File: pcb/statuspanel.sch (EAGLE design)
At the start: 3 parts

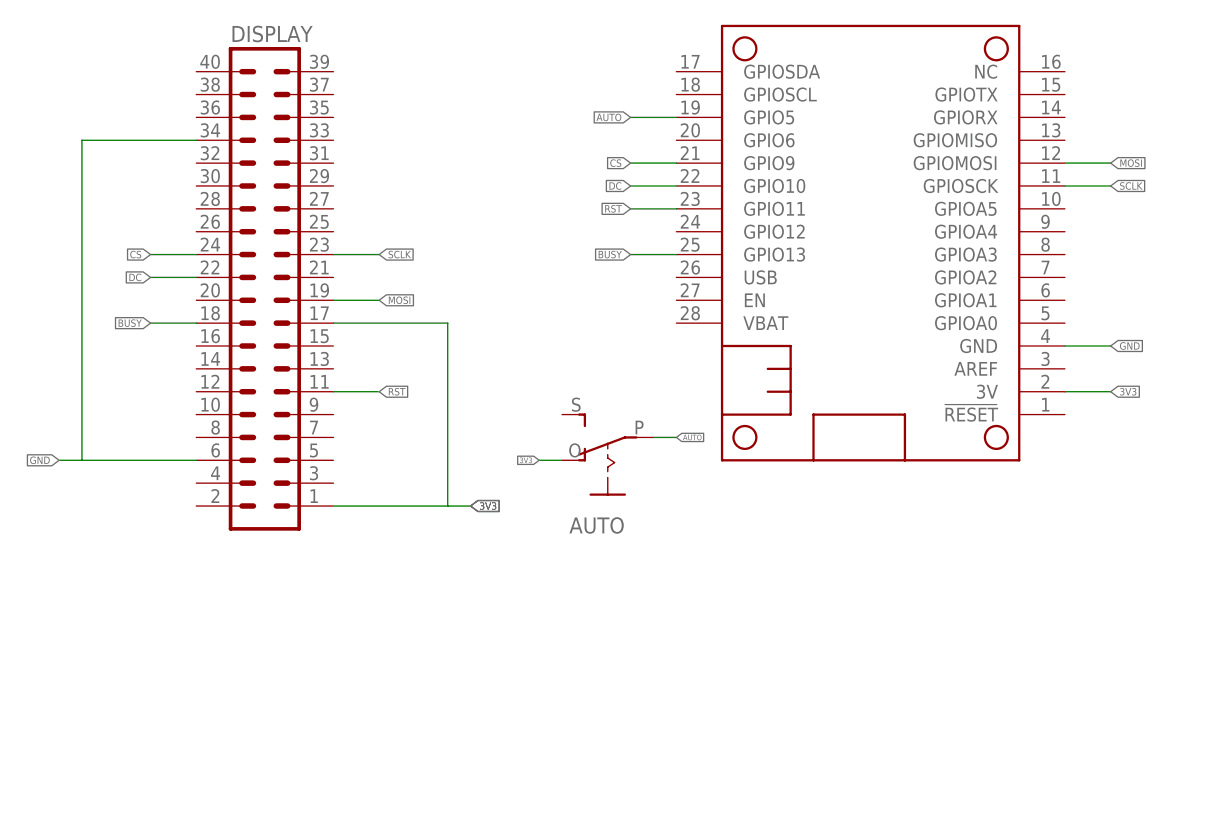
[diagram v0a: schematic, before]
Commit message: Update the PCB to add an unpair button
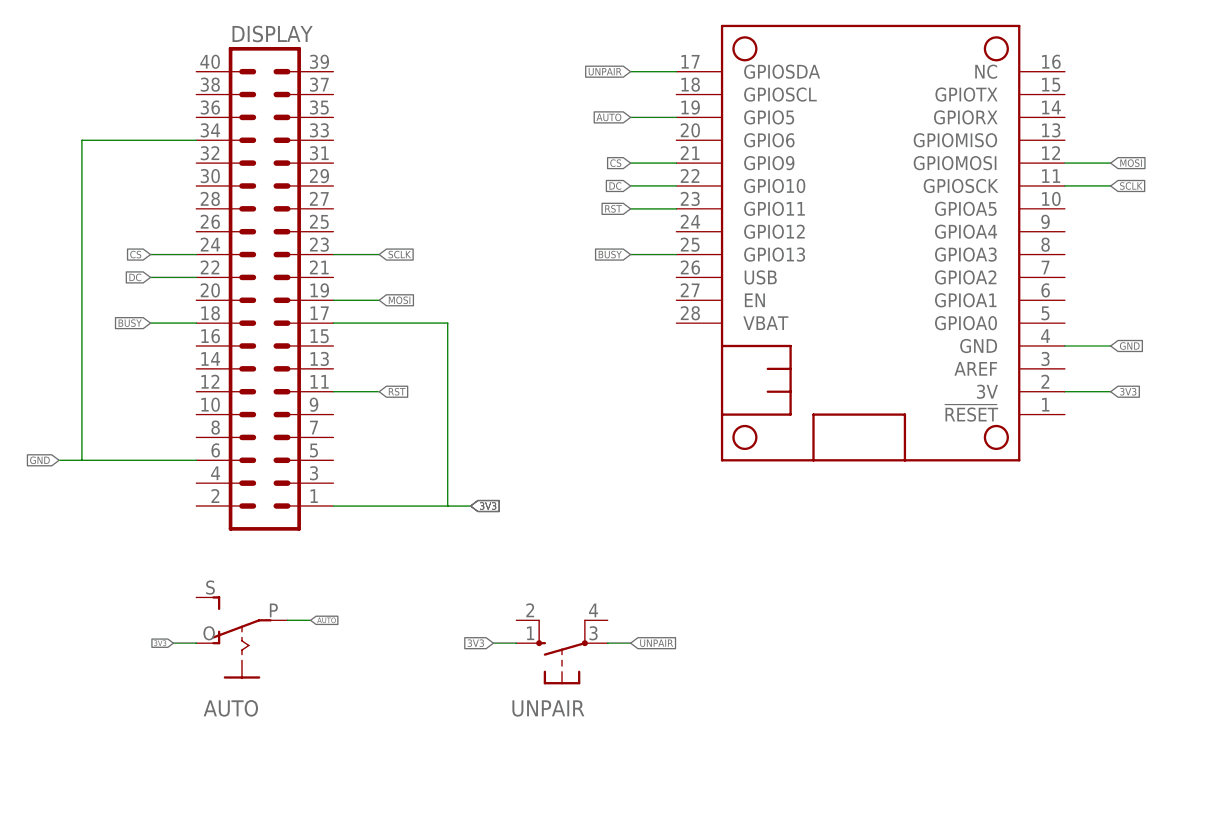
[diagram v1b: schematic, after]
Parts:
- added UNPAIR: (no value), switch-omron:10-XX
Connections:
- new net UNPAIR: HUZZAH32.GPIOSDA, UNPAIR.P
- net 3V3: now also UNPAIR.S
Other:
- moved on the sheet: AUTO
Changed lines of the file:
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@@
 <?xml version="1.0" encoding="utf-8"?>
 <!DOCTYPE eagle SYSTEM "eagle.dtd">
-<eagle version="9.2.2">
+<eagle version="9.5.2">
 <drawing>
 <settings>
@@
 <part name="DISPLAY" library="con-lstb" library_urn="urn:adsk.eagle:library:162" deviceset="MA20-2" device="" package3d_urn="urn:adsk.eagle:package:8338/1"/>
 <part name="AUTO" library="adafruit" library_urn="urn:adsk.eagle:library:420" deviceset="EG1218" device="S" package3d_urn="urn:adsk.eagle:package:6240649/1"/>
+<part name="UNPAIR" library="switch-omron" library_urn="urn:adsk.eagle:library:377" deviceset="10-XX" device="" package3d_urn="urn:adsk.eagle:package:27496/1"/>
 </parts>
 <sheets>
@@
 <attribute name="NAME" x="41.91" y="89.662" size="1.778" layer="95"/>
 </instance>
-<instance part="AUTO" gate="1" x="83.82" y="43.18" smashed="yes" rot="R90">
-<attribute name="NAME" x="85.725" y="36.83" size="1.778" layer="95" rot="R180"/>
-<attribute name="VALUE" x="80.645" y="39.37" size="1.778" layer="96" rot="R180"/>
+<instance part="AUTO" gate="1" x="43.18" y="22.86" smashed="yes" rot="R90">
+<attribute name="NAME" x="45.085" y="16.51" size="1.778" layer="95" rot="R180"/>
+<attribute name="VALUE" x="40.005" y="19.05" size="1.778" layer="96" rot="R180"/>
+</instance>
+<instance part="UNPAIR" gate="1" x="78.74" y="22.86" smashed="yes" rot="R90">
+<attribute name="NAME" x="81.28" y="16.51" size="1.778" layer="95" rot="R180"/>
+<attribute name="VALUE" x="75.565" y="19.05" size="1.778" layer="96" rot="R180"/>
 </instance>
 </instances>
@@
 <segment>
 <pinref part="AUTO" gate="1" pin="O"/>
-<wire x1="78.74" y1="43.18" x2="76.2" y2="43.18" width="0.1524" layer="91"/>
-<label x="76.2" y="43.18" size="0.6096" layer="95" rot="R180" xref="yes"/>
+<wire x1="38.1" y1="22.86" x2="35.56" y2="22.86" width="0.1524" layer="91"/>
+<label x="35.56" y="22.86" size="0.6096" layer="95" rot="R180" xref="yes"/>
+</segment>
+<segment>
+<pinref part="UNPAIR" gate="1" pin="S"/>
+<wire x1="73.66" y1="22.86" x2="71.12" y2="22.86" width="0.1524" layer="91"/>
+<label x="71.12" y="22.86" size="0.8128" layer="95" rot="R180" xref="yes"/>
 </segment>
 </net>
@@
 <segment>
 <pinref part="AUTO" gate="1" pin="P"/>
-<wire x1="88.9" y1="45.72" x2="91.44" y2="45.72" width="0.1524" layer="91"/>
-<label x="91.44" y="45.72" size="0.6096" layer="95" xref="yes"/>
-</segment>
-</net>
+<wire x1="48.26" y1="25.4" x2="50.8" y2="25.4" width="0.1524" layer="91"/>
+<label x="50.8" y="25.4" size="0.6096" layer="95" xref="yes"/>
+</segment>
+</net>
+<net name="UNPAIR" class="0">
+<segment>
+<pinref part="HUZZAH32" gate="G$1" pin="GPIOSDA"/>
+<wire x1="91.44" y1="86.36" x2="86.36" y2="86.36" width="0.1524" layer="91"/>
+<label x="86.36" y="86.36" size="0.8128" layer="95" rot="R180" xref="yes"/>
+</segment>
+<segment>
+<pinref part="UNPAIR" gate="1" pin="P"/>
+<wire x1="83.82" y1="22.86" x2="86.36" y2="22.86" width="0.1524" layer="91"/>
+<label x="86.36" y="22.86" size="0.8128" layer="95" xref="yes"/>
+</segment>
+</net>

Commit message: Rename RST to PANELRESET
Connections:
- net RST renamed PANELRESET
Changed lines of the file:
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@@
 </busses>
 <nets>
-<net name="RST" class="0">
+<net name="PANELRESET" class="0">
 <segment>
 <pinref part="DISPLAY" gate="G$1" pin="11"/>
-<wire x1="53.34" y1="50.8" x2="58.42" y2="50.8" width="0.1524" layer="91"/>
-<label x="58.42" y="50.8" size="0.8128" layer="95" xref="yes"/>
+<wire x1="53.34" y1="50.8" x2="55.88" y2="50.8" width="0.1524" layer="91"/>
+<label x="55.88" y="50.8" size="0.8128" layer="95" xref="yes"/>
 </segment>
 <segment>

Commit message: Update the wire for unpair
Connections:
- net UNPAIR: now also HUZZAH32.GPIOA2; no longer HUZZAH32.GPIOSDA
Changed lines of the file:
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@@
 <net name="UNPAIR" class="0">
-<segment>
-<pinref part="HUZZAH32" gate="G$1" pin="GPIOSDA"/>
-<wire x1="91.44" y1="86.36" x2="86.36" y2="86.36" width="0.1524" layer="91"/>
-<label x="86.36" y="86.36" size="0.8128" layer="95" rot="R180" xref="yes"/>
-</segment>
 <segment>
 <pinref part="UNPAIR" gate="1" pin="P"/>
@@
 <label x="86.36" y="22.86" size="0.8128" layer="95" xref="yes"/>
 </segment>
+<segment>
+<pinref part="HUZZAH32" gate="G$1" pin="GPIOA2"/>
+<wire x1="134.62" y1="63.5" x2="139.7" y2="63.5" width="0.1524" layer="91"/>
+<label x="139.7" y="63.5" size="0.8128" layer="95" xref="yes"/>
+</segment>
 </net>

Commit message: Add an LED
I’m not doing anything with this yet.
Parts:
- added STAT.: (no value), adafruit:LED3MM
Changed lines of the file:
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@@
 <part name="AUTO" library="adafruit" library_urn="urn:adsk.eagle:library:420" deviceset="EG1218" device="S" package3d_urn="urn:adsk.eagle:package:6240649/1"/>
 <part name="UNPAIR" library="switch-omron" library_urn="urn:adsk.eagle:library:377" deviceset="10-XX" device="" package3d_urn="urn:adsk.eagle:package:27496/1"/>
+<part name="STAT." library="adafruit" library_urn="urn:adsk.eagle:library:420" deviceset="LED" device="3MM" package3d_urn="urn:adsk.eagle:package:6240537/1"/>
 </parts>
 <sheets>
@@
 <attribute name="VALUE" x="75.565" y="19.05" size="1.778" layer="96" rot="R180"/>
 </instance>
+<instance part="STAT." gate="G$1" x="109.22" y="22.86" smashed="yes" rot="R270">
+<attribute name="NAME" x="104.648" y="16.764" size="1.778" layer="95"/>
+<attribute name="VALUE" x="104.648" y="17.145" size="1.778" layer="96"/>
+</instance>
 </instances>

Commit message: Connect up one leg of the LED
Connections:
- new net N$3: STAT..C
- new net STATUS: HUZZAH32.NC, STAT..A
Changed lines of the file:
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@@
+</segment>
+</net>
+<net name="STATUS" class="0">
+<segment>
+<pinref part="STAT." gate="G$1" pin="A"/>
+<wire x1="111.76" y1="22.86" x2="114.3" y2="22.86" width="0.1524" layer="91"/>
+<label x="114.3" y="22.86" size="0.8128" layer="95" xref="yes"/>
+</segment>
+<segment>
+<pinref part="HUZZAH32" gate="G$1" pin="NC"/>
+<wire x1="134.62" y1="86.36" x2="139.7" y2="86.36" width="0.1524" layer="91"/>
+<label x="139.7" y="86.36" size="0.8128" layer="95" xref="yes"/>
+</segment>
+</net>
+<net name="N$3" class="0">
+<segment>
+<pinref part="STAT." gate="G$1" pin="C"/>
+<wire x1="104.14" y1="22.86" x2="101.6" y2="22.86" width="0.1524" layer="91"/>
 </segment>
 </net>

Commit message: Move un-pair to GPIO 32 / Adafruit-GPIO6.
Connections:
- net UNPAIR: now also HUZZAH32.GPIO6; no longer HUZZAH32.GPIOA2
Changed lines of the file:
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@@
 </segment>
 <segment>
-<pinref part="HUZZAH32" gate="G$1" pin="GPIOA2"/>
-<wire x1="134.62" y1="63.5" x2="139.7" y2="63.5" width="0.1524" layer="91"/>
-<label x="139.7" y="63.5" size="0.8128" layer="95" xref="yes"/>
+<pinref part="HUZZAH32" gate="G$1" pin="GPIO6"/>
+<wire x1="91.44" y1="78.74" x2="86.36" y2="78.74" width="0.1524" layer="91"/>
+<label x="86.36" y="78.74" size="0.8128" layer="95" rot="R180" xref="yes"/>
 </segment>
 </net>

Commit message: Add the resistors to the board
- Divider
- Status LED
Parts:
- added R1: 5.1, adafruit:R-US_0411/12
- added R2, R3: 4.7K, adafruit:R-US_0411/12
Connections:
- new net USB: HUZZAH32.USB, R2.2
- new net USBDETECT: HUZZAH32.GPIOA3, R2.1, R3.2
- net GND: now also R1.1, R3.1
- net N$3: now also R1.2
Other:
- moved on the sheet: AUTO, STAT., UNPAIR
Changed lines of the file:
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@@
 <part name="UNPAIR" library="switch-omron" library_urn="urn:adsk.eagle:library:377" deviceset="10-XX" device="" package3d_urn="urn:adsk.eagle:package:27496/1"/>
 <part name="STAT." library="adafruit" library_urn="urn:adsk.eagle:library:420" deviceset="LED" device="3MM" package3d_urn="urn:adsk.eagle:package:6240537/1"/>
+<part name="R1" library="adafruit" library_urn="urn:adsk.eagle:library:420" deviceset="R-US_" device="0411/12" package3d_urn="urn:adsk.eagle:package:6240605/1" value="5.1"/>
+<part name="R2" library="adafruit" library_urn="urn:adsk.eagle:library:420" deviceset="R-US_" device="0411/12" package3d_urn="urn:adsk.eagle:package:6240605/1" value="4.7K"/>
+<part name="R3" library="adafruit" library_urn="urn:adsk.eagle:library:420" deviceset="R-US_" device="0411/12" package3d_urn="urn:adsk.eagle:package:6240605/1" value="4.7K"/>
 </parts>
 <sheets>
@@
 <attribute name="NAME" x="41.91" y="89.662" size="1.778" layer="95"/>
 </instance>
-<instance part="AUTO" gate="1" x="43.18" y="22.86" smashed="yes" rot="R90">
-<attribute name="NAME" x="45.085" y="16.51" size="1.778" layer="95" rot="R180"/>
-<attribute name="VALUE" x="40.005" y="19.05" size="1.778" layer="96" rot="R180"/>
-</instance>
-<instance part="UNPAIR" gate="1" x="78.74" y="22.86" smashed="yes" rot="R90">
-<attribute name="NAME" x="81.28" y="16.51" size="1.778" layer="95" rot="R180"/>
-<attribute name="VALUE" x="75.565" y="19.05" size="1.778" layer="96" rot="R180"/>
-</instance>
-<instance part="STAT." gate="G$1" x="109.22" y="22.86" smashed="yes" rot="R270">
-<attribute name="NAME" x="104.648" y="16.764" size="1.778" layer="95"/>
-<attribute name="VALUE" x="104.648" y="17.145" size="1.778" layer="96"/>
+<instance part="AUTO" gate="1" x="35.56" y="20.32" smashed="yes" rot="R90">
+<attribute name="NAME" x="37.465" y="13.97" size="1.778" layer="95" rot="R180"/>
+<attribute name="VALUE" x="32.385" y="16.51" size="1.778" layer="96" rot="R180"/>
+</instance>
+<instance part="UNPAIR" gate="1" x="68.58" y="20.32" smashed="yes" rot="R90">
+<attribute name="NAME" x="71.12" y="13.97" size="1.778" layer="95" rot="R180"/>
+<attribute name="VALUE" x="65.405" y="16.51" size="1.778" layer="96" rot="R180"/>
+</instance>
+<instance part="STAT." gate="G$1" x="119.38" y="30.48" smashed="yes" rot="R270">
+<attribute name="NAME" x="114.808" y="24.384" size="1.778" layer="95"/>
+<attribute name="VALUE" x="114.808" y="24.765" size="1.778" layer="96"/>
+</instance>
+<instance part="R1" gate="G$1" x="106.68" y="30.48" smashed="yes">
+<attribute name="NAME" x="102.87" y="31.9786" size="1.778" layer="95"/>
+<attribute name="VALUE" x="102.87" y="27.178" size="1.778" layer="96"/>
+</instance>
+<instance part="R2" gate="G$1" x="121.92" y="15.24" smashed="yes">
+<attribute name="NAME" x="118.11" y="16.7386" size="1.778" layer="95"/>
+<attribute name="VALUE" x="118.11" y="11.938" size="1.778" layer="96"/>
+</instance>
+<instance part="R3" gate="G$1" x="106.68" y="15.24" smashed="yes">
+<attribute name="NAME" x="102.87" y="16.7386" size="1.778" layer="95"/>
+<attribute name="VALUE" x="102.87" y="11.938" size="1.778" layer="96"/>
 </instance>
 </instances>
@@
 <segment>
 <pinref part="AUTO" gate="1" pin="O"/>
-<wire x1="38.1" y1="22.86" x2="35.56" y2="22.86" width="0.1524" layer="91"/>
-<label x="35.56" y="22.86" size="0.6096" layer="95" rot="R180" xref="yes"/>
+<wire x1="30.48" y1="20.32" x2="27.94" y2="20.32" width="0.1524" layer="91"/>
+<label x="27.94" y="20.32" size="0.6096" layer="95" rot="R180" xref="yes"/>
 </segment>
 <segment>
 <pinref part="UNPAIR" gate="1" pin="S"/>
-<wire x1="73.66" y1="22.86" x2="71.12" y2="22.86" width="0.1524" layer="91"/>
-<label x="71.12" y="22.86" size="0.8128" layer="95" rot="R180" xref="yes"/>
+<wire x1="63.5" y1="20.32" x2="60.96" y2="20.32" width="0.1524" layer="91"/>
+<label x="60.96" y="20.32" size="0.8128" layer="95" rot="R180" xref="yes"/>
 </segment>
 </net>
@@
 <label x="139.7" y="55.88" size="0.8128" layer="95" xref="yes"/>
 </segment>
+<segment>
+<pinref part="R1" gate="G$1" pin="1"/>
+<wire x1="101.6" y1="30.48" x2="99.06" y2="30.48" width="0.1524" layer="91"/>
+<label x="99.06" y="30.48" size="0.8128" layer="95" rot="R180" xref="yes"/>
+</segment>
+<segment>
+<pinref part="R3" gate="G$1" pin="1"/>
+<wire x1="101.6" y1="15.24" x2="99.06" y2="15.24" width="0.1524" layer="91"/>
+<label x="99.06" y="15.24" size="0.8128" layer="95" rot="R180" xref="yes"/>
+</segment>
 </net>
 <net name="AUTO" class="0">
@@
 <segment>
 <pinref part="AUTO" gate="1" pin="P"/>
-<wire x1="48.26" y1="25.4" x2="50.8" y2="25.4" width="0.1524" layer="91"/>
-<label x="50.8" y="25.4" size="0.6096" layer="95" xref="yes"/>
+<wire x1="40.64" y1="22.86" x2="43.18" y2="22.86" width="0.1524" layer="91"/>
+<label x="43.18" y="22.86" size="0.6096" layer="95" xref="yes"/>
 </segment>
 </net>
@@
 <segment>
 <pinref part="UNPAIR" gate="1" pin="P"/>
-<wire x1="83.82" y1="22.86" x2="86.36" y2="22.86" width="0.1524" layer="91"/>
-<label x="86.36" y="22.86" size="0.8128" layer="95" xref="yes"/>
+<wire x1="73.66" y1="20.32" x2="76.2" y2="20.32" width="0.1524" layer="91"/>
+<label x="76.2" y="20.32" size="0.8128" layer="95" xref="yes"/>
 </segment>
 <segment>
@@
 <segment>
 <pinref part="STAT." gate="G$1" pin="A"/>
-<wire x1="111.76" y1="22.86" x2="114.3" y2="22.86" width="0.1524" layer="91"/>
-<label x="114.3" y="22.86" size="0.8128" layer="95" xref="yes"/>
+<wire x1="121.92" y1="30.48" x2="124.46" y2="30.48" width="0.1524" layer="91"/>
+<label x="124.46" y="30.48" size="0.8128" layer="95" xref="yes"/>
 </segment>
 <segment>
@@
 <segment>
 <pinref part="STAT." gate="G$1" pin="C"/>
-<wire x1="104.14" y1="22.86" x2="101.6" y2="22.86" width="0.1524" layer="91"/>
-</segment>
-</net>
+<wire x1="114.3" y1="30.48" x2="111.76" y2="30.48" width="0.1524" layer="91"/>
+<pinref part="R1" gate="G$1" pin="2"/>
+</segment>
+</net>
+<net name="USB" class="0">
+<segment>
+<pinref part="HUZZAH32" gate="G$1" pin="USB"/>
+<wire x1="91.44" y1="63.5" x2="86.36" y2="63.5" width="0.1524" layer="91"/>
+<label x="86.36" y="63.5" size="0.8128" layer="95" rot="R180" xref="yes"/>
+</segment>
+<segment>
+<pinref part="R2" gate="G$1" pin="2"/>
+<wire x1="127" y1="15.24" x2="129.54" y2="15.24" width="0.1524" layer="91"/>
+<label x="129.54" y="15.24" size="0.8128" layer="95" xref="yes"/>
+</segment>
+</net>
+<net name="USBDETECT" class="0">
+<segment>
+<pinref part="HUZZAH32" gate="G$1" pin="GPIOA3"/>
+<wire x1="134.62" y1="66.04" x2="139.7" y2="66.04" width="0.1524" layer="91"/>
+<label x="139.7" y="66.04" size="0.8128" layer="95" xref="yes"/>
+</segment>
+<segment>
+<pinref part="R2" gate="G$1" pin="1"/>
+<pinref part="R3" gate="G$1" pin="2"/>
+<wire x1="116.84" y1="15.24" x2="114.3" y2="15.24" width="0.1524" layer="91"/>
+<junction x="114.3" y="15.24"/>
+<wire x1="114.3" y1="15.24" x2="111.76" y2="15.24" width="0.1524" layer="91"/>
+<wire x1="114.3" y1="15.24" x2="114.3" y2="12.7" width="0.1524" layer="91"/>
+<label x="114.3" y="12.7" size="0.8128" layer="95" rot="R270" xref="yes"/>
+</segment>
+</net>

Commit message: Update the PCB to tie 5V and 3V3 together to account for the new display controller board.
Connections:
- net 3V3: now also DISPLAY.2, DISPLAY.4
- net GND: now also DISPLAY.14, DISPLAY.20, DISPLAY.25, DISPLAY.30, DISPLAY.9
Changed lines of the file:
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@@
 <?xml version="1.0" encoding="utf-8"?>
 <!DOCTYPE eagle SYSTEM "eagle.dtd">
-<eagle version="9.5.2">
+<eagle version="9.6.2">
 <drawing>
 <settings>
@@
 <label x="60.96" y="20.32" size="0.8128" layer="95" rot="R180" xref="yes"/>
 </segment>
+<segment>
+<pinref part="DISPLAY" gate="G$1" pin="4"/>
+<wire x1="38.1" y1="40.64" x2="33.02" y2="40.64" width="0.1524" layer="91"/>
+<pinref part="DISPLAY" gate="G$1" pin="2"/>
+<wire x1="38.1" y1="38.1" x2="33.02" y2="38.1" width="0.1524" layer="91"/>
+<wire x1="33.02" y1="38.1" x2="30.48" y2="38.1" width="0.1524" layer="91"/>
+<wire x1="33.02" y1="40.64" x2="33.02" y2="38.1" width="0.1524" layer="91"/>
+<label x="30.48" y="38.1" size="0.8128" layer="95" rot="R180" xref="yes"/>
+</segment>
 </net>
 <net name="GND" class="0">
@@
 <wire x1="25.4" y1="43.18" x2="22.86" y2="43.18" width="0.1524" layer="91"/>
 <wire x1="38.1" y1="78.74" x2="25.4" y2="78.74" width="0.1524" layer="91"/>
-<wire x1="25.4" y1="78.74" x2="25.4" y2="43.18" width="0.1524" layer="91"/>
+<wire x1="25.4" y1="78.74" x2="25.4" y2="73.66" width="0.1524" layer="91"/>
 <label x="22.86" y="43.18" size="0.8128" layer="95" rot="R180" xref="yes"/>
+<pinref part="DISPLAY" gate="G$1" pin="30"/>
+<wire x1="25.4" y1="73.66" x2="25.4" y2="60.96" width="0.1524" layer="91"/>
+<wire x1="25.4" y1="60.96" x2="25.4" y2="53.34" width="0.1524" layer="91"/>
+<wire x1="25.4" y1="53.34" x2="25.4" y2="43.18" width="0.1524" layer="91"/>
+<wire x1="38.1" y1="73.66" x2="25.4" y2="73.66" width="0.1524" layer="91"/>
+<pinref part="DISPLAY" gate="G$1" pin="20"/>
+<wire x1="38.1" y1="60.96" x2="25.4" y2="60.96" width="0.1524" layer="91"/>
+<pinref part="DISPLAY" gate="G$1" pin="14"/>
+<wire x1="38.1" y1="53.34" x2="25.4" y2="53.34" width="0.1524" layer="91"/>
 </segment>
 <segment>
@@
 <label x="99.06" y="15.24" size="0.8128" layer="95" rot="R180" xref="yes"/>
 </segment>
-</net>
+<segment>
+<pinref part="DISPLAY" gate="G$1" pin="9"/>
+<wire x1="53.34" y1="48.26" x2="55.88" y2="48.26" width="0.1524" layer="91"/>
+<label x="55.88" y="48.26" size="0.8128" layer="95" xref="yes"/>
+</segment>
+<segment>
+<pinref part="DISPLAY" gate="G$1" pin="25"/>
+<wire x1="53.34" y1="68.58" x2="58.42" y2="68.58" width="0.1524" layer="91"/>
+<label x="58.42" y="68.58" size="0.8128" layer="95" xref="yes"/>
+</segment>
+</net>
